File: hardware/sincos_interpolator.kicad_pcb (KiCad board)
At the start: 2 copper layers, 100 x 50 mm, 53 parts, among them J1 SIN, J10 RJ45_Shielded, J2 COS, J3 ZERO, J4 POWER IN, J5 POWER OUT, J6 A, J7 B, J8 Z, J9 RJ45_Shielded, Q1 TIC116, U1 iC-NV, U2 MC3487DX

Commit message: New component references and fab outputs
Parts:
- JP11: renamed from JP6; value SIN_VREF -> SIN VREF
- JP21: renamed from JP7; value COS_VREF -> COS VREF
- renumbered D4 to D11, D5 to D21, D6 to D31, J4 to J1, J1 to J11, J6 to J12, J5 to J2, J2 to J21, J7 to J22, J10 to J3, J3 to J31, J8 to J32, J9 to J4, JP9 to JP12, JP12 to JP13, JP10 to JP22, JP13 to JP23, JP11 to JP32, JP14 to JP33, JP8 to JP6, R5 to R1, R1 to R11, R2 to R12, R8 to R13, R6 to R2, R3 to R21, R4 to R22, R9 to R23, R7 to R3, R10 to R33
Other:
- board text added: "2023-08-20 Rev. 1.2"
- board text added: "VREF COS"
- board text added: "VREF SIN"
- board text removed: "2023-08-19 Rev. 1.1"
- board text removed: "VREF"

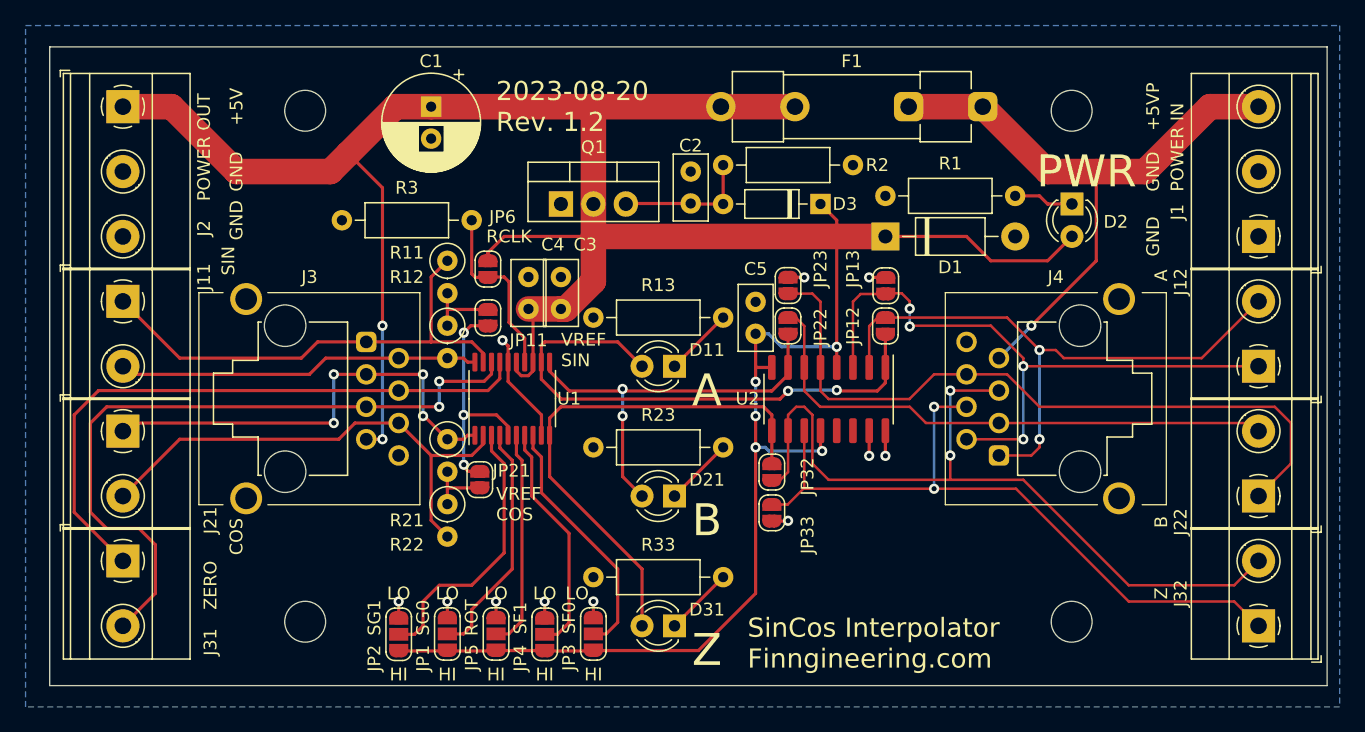
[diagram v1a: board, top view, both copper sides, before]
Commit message: Corrected MC3487DX power polarity and separated shield
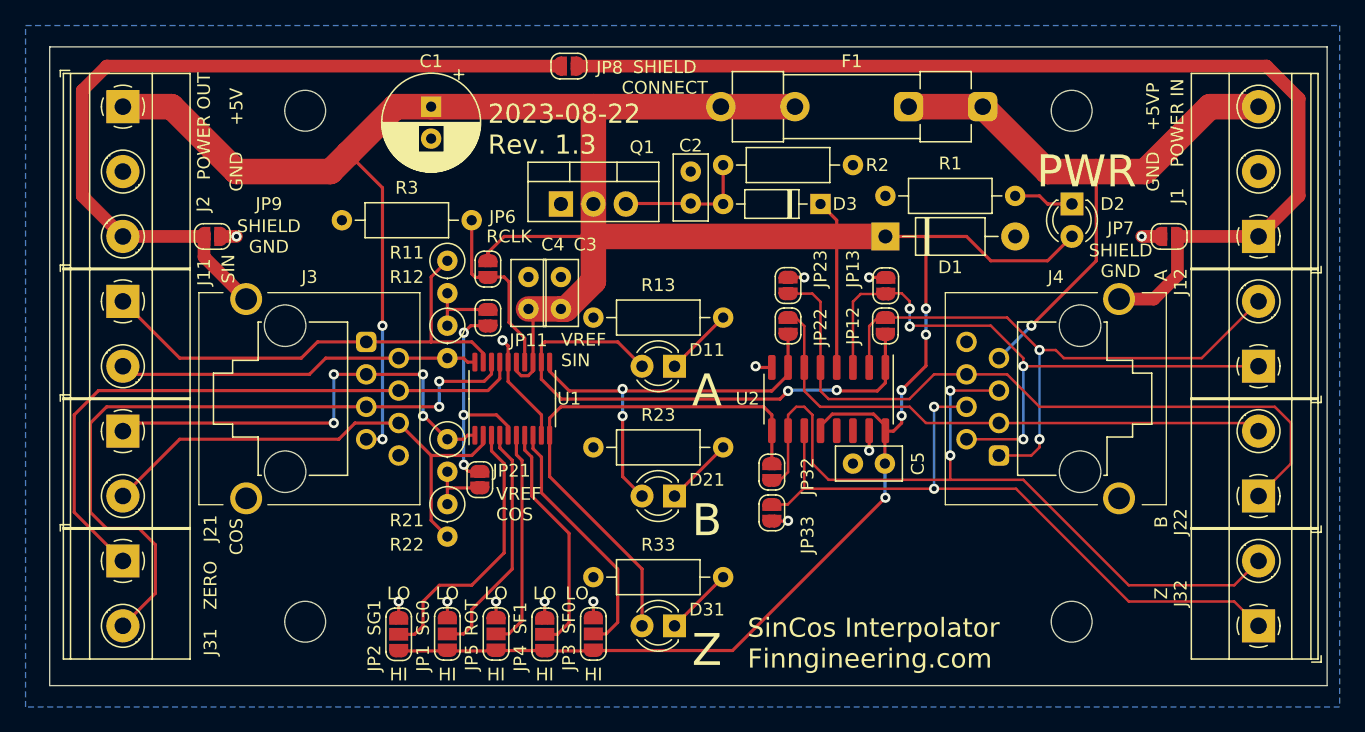
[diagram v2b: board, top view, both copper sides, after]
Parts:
- added JP7: SHIELD GND, Jumper:SolderJumper-2_P1.3mm_Open_RoundedPad1.0x1.5mm, F.Cu at (207.6, 116.8)
- added JP8: SHIELD CONNECT, Jumper:SolderJumper-2_P1.3mm_Open_RoundedPad1.0x1.5mm, F.Cu at (160.6, 103.5)
- added JP9: SHIELD GND, Jumper:SolderJumper-2_P1.3mm_Open_RoundedPad1.0x1.5mm, F.Cu at (132.7, 116.8)
- moved C5 12.7 mm to (182.9, 134.6), turned to 0 degrees
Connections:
- C5 pad 1: +5V -> GND
- C5 pad 2: GND -> +5V
- J1 pad 1: GND -> /SHIELD_IN
- J2 pad 3: GND -> /SHIELD_OUT
- J3 pad SH: GND -> /SHIELD_OUT
- J4 pad SH: GND -> /SHIELD_IN
- U2 pad 16: GND -> +5V
- U2 pad 8: +5V -> GND
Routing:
- net /SHIELD_IN: track 0.00 -> 84.4 mm
- net /SHIELD_OUT: track 0.00 -> 63.6 mm
- net +5V: track 234.5 -> 241.3 mm
- net GND: track 22.8 -> 24.5 mm, vias 11 -> 13
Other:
- board text added: "2023-08-22 Rev. 1.3"
- board text added: "SHIELD CONNECT"
- board text added: "SHIELD GND"
- board text removed: "2023-08-20 Rev. 1.2"

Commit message: RJ45 jacks rotated 180 degrees
RJ45 jacks rotated 180 degrees to allow the used of angled RJ45 jacks
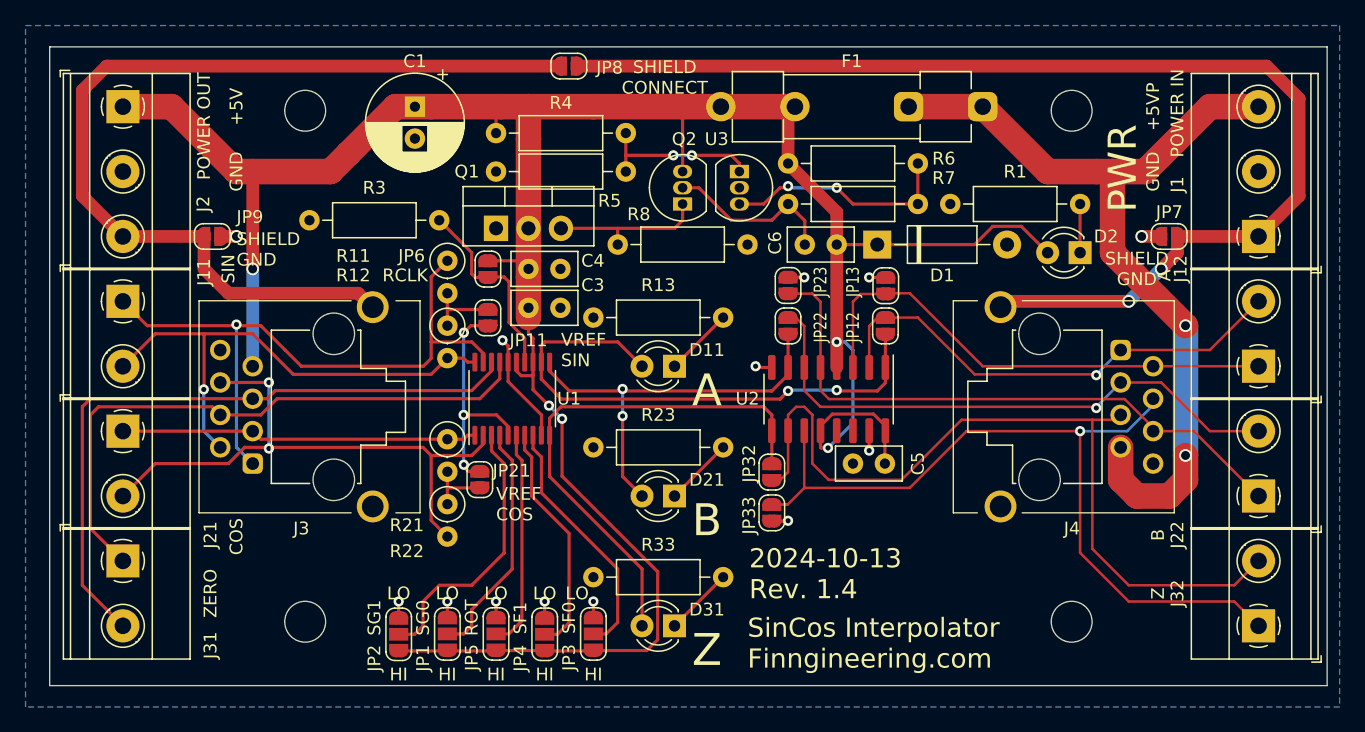
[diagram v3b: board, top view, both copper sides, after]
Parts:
- removed C2: 10n, Capacitor_THT:C_Disc_D5.0mm_W2.5mm_P2.50mm
- removed D3: 5V1, Diode_THT:D_DO-35_SOD27_P7.62mm_Horizontal
- removed R2: 1k, Resistor_THT:R_Axial_DIN0207_L6.3mm_D2.5mm_P10.16mm_Horizontal
- added C6: 100n, Capacitor_THT:C_Disc_D5.0mm_W2.5mm_P2.50mm, F.Cu at (181.6, 117.5)
- added Q2: BC557, Package_TO_SOT_THT:TO-92_Inline, F.Cu at (169.5, 114.3)
- added R4: 12k, Resistor_THT:R_Axial_DIN0207_L6.3mm_D2.5mm_P10.16mm_Horizontal, F.Cu at (154.9, 108.8)
- added R5: 10k, Resistor_THT:R_Axial_DIN0207_L6.3mm_D2.5mm_P10.16mm_Horizontal, F.Cu at (165.1, 111.8)
- added R6: 100, Resistor_THT:R_Axial_DIN0207_L6.3mm_D2.5mm_P10.16mm_Horizontal, F.Cu at (177.8, 111.1)
- added R7: 1k, Resistor_THT:R_Axial_DIN0207_L6.3mm_D2.5mm_P10.16mm_Horizontal, F.Cu at (188.0, 114.3)
- added R8: 1k, Resistor_THT:R_Axial_DIN0207_L6.3mm_D2.5mm_P10.16mm_Horizontal, F.Cu at (164.5, 117.5)
- added U3: TL431LP, Package_TO_SOT_THT:TO-92_Inline, F.Cu at (174.0, 111.8)
- JP12: value A SINGLE ENDED -> A SINGLE
- JP22: value B SINGLE ENDED -> B SINGLE
- moved J4 14.6 mm to (206.4, 130.2), turned to 180 degrees
- moved J3 14.0 mm to (133.3, 130.2), turned to 0 degrees
- moved Q1 5.43 mm to (154.9, 116.2)
- moved R1 5.12 mm to (200.7, 114.3)
- moved D2 3.87 mm to (200.7, 118.1), turned to 180 degrees
- moved C4 3.14 mm to (157.5, 119.4), turned to 0 degrees
- moved C3 2.54 mm to (157.5, 122.4), turned to 0 degrees
- moved R3 2.54 mm to (150.5, 115.6)
- moved C1 1.27 mm to (148.6, 106.7)
- moved D1 0.90 mm to (184.8, 117.5)
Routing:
- net +5V: track 241.3 -> 212.2 mm, vias 7 -> 5
- net Net-(R6-Pad2): track 0.00 -> 18.3 mm, vias 0 -> 2
- net +5VP: track 49.4 -> 66.8 mm, vias 1 -> 2
- net Net-(C6-Pad2): track 0.00 -> 13.6 mm
- net Net-(R4-Pad2): track 0.00 -> 12.8 mm, vias 0 -> 2
- net /PSIN: track 38.5 -> 51.3 mm, vias 0 -> 1
- net /A-: track 51.3 -> 39.5 mm, vias 4 -> 0
- net /NSIN: track 28.5 -> 40.0 mm, vias 0 -> 1
- net /SHIELD_OUT: track 63.6 -> 74.3 mm
- net /A+: track 48.2 -> 38.3 mm, vias 2 -> 1
- net /SHIELD_IN: track 84.4 -> 92.9 mm, vias 0 -> 2
- net /B-: track 56.0 -> 47.6 mm
- net /PCOS: track 35.8 -> 27.9 mm, vias 4 -> 0
- net /NCOS: track 39.6 -> 47.0 mm, vias 0 -> 2
- net /Z-: track 56.5 -> 63.9 mm, vias 2 -> 1
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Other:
- board text added: "2024-10-13 Rev. 1.4"
- board text added: "ENDED"
- board text removed: "2023-08-22 Rev. 1.3"
